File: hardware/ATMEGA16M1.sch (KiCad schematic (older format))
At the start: 44 parts, among them IC1 ATMEGA16M1-A, IC2 MCP2551-I/SN, J1 PWR, J2 USB, J3 RELAY, J4 RELAY, J5 RELAY, J6 GPIO, J7 AMP/D2A, J8 ADC, J9 CAN, SW1 SW_PUSH, U1 NCP1117ST50T3G, U2 FT232RL, U3 RELAY_VO14642AT, U4 RELAY_VO14642AT, U5 RELAY_VO14642AT, X1 16MHz

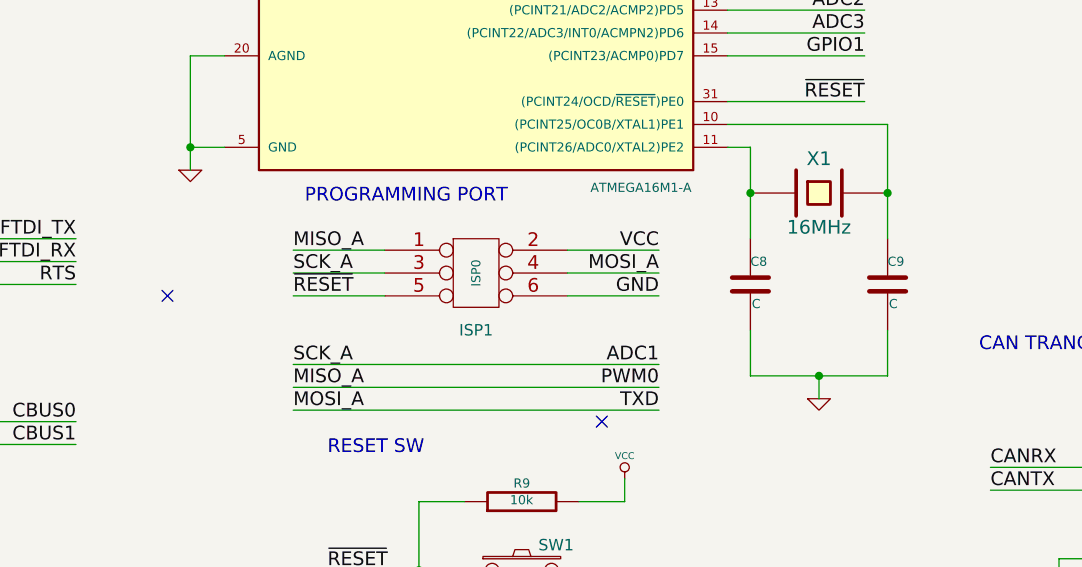
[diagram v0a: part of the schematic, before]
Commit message: PCB revisions: schematic update, cvpcb, pcb component grouping
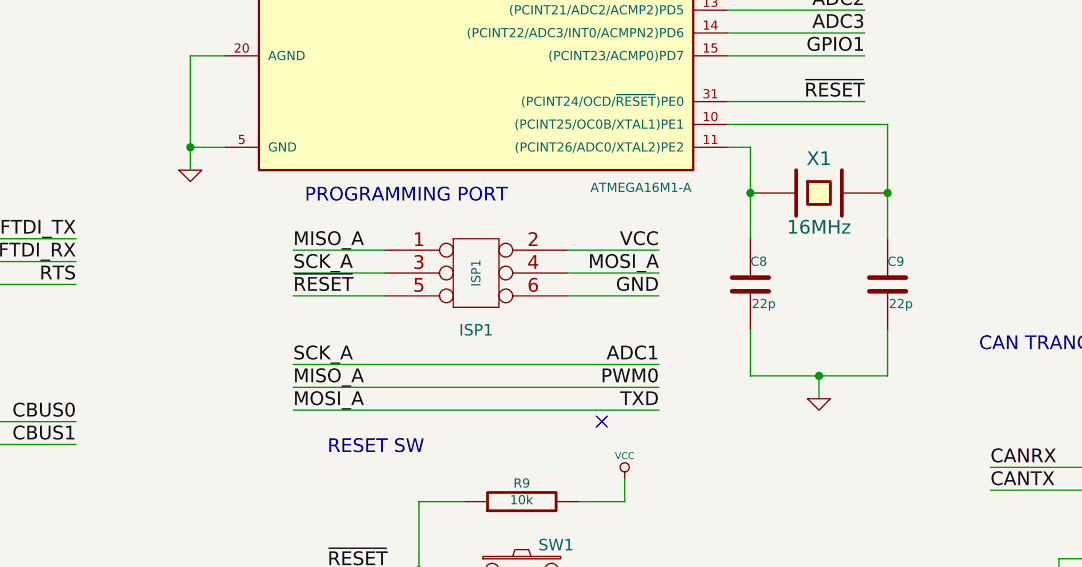
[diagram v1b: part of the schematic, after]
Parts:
- C8, C9: value C -> 22p
- ISP1: value ISP0 -> ISP1
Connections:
- no-connect marks 18 -> 17
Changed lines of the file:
@@
 Sheet 1 1
 Title "LFEF CAN Communication Board"
-Date "10 mar 2015"
+Date "23 mar 2015"
 Rev "0"
 Comp "Lafayette College"
@@
 P 6350 4700
 F 0 "C8" H 6350 4800 40  0000 L CNN
-F 1 "C" H 6356 4615 40  0000 L CNN
+F 1 "22p" H 6356 4615 40  0000 L CNN
 F 2 "~" H 6388 4550 30  0000 C CNN
 F 3 "~" H 6350 4700 60  0000 C CNN
@@
 P 6950 4700
 F 0 "C9" H 6950 4800 40  0000 L CNN
-F 1 "C" H 6956 4615 40  0000 L CNN
+F 1 "22p" H 6956 4615 40  0000 L CNN
 F 2 "~" H 6988 4550 30  0000 C CNN
 F 3 "~" H 6950 4700 60  0000 C CNN
@@
 P 5150 4700
 F 0 "ISP1" H 5150 4500 50  0000 C CNN
-F 1 "ISP0" V 5150 4750 40  0000 C CNN
+F 1 "ISP1" V 5150 4750 40  0000 C CNN
 F 2 "~" H 5150 4700 60  0000 C CNN
 F 3 "~" H 5150 4700 60  0000 C CNN
@@
 I/O HEADERS
 NoConn ~ 9650 4000
-NoConn ~ 3800 4750
 NoConn ~ 5700 5300
 $Comp

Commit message: PCB rough initial layout
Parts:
- added R11, R12, R13: 220, ~, symbol R
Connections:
- net GND: now also J7.8
- net SSR0: now also R11.1; no longer U3.1 (A)
- net SSR1: now also R12.1; no longer U4.1 (A)
- net SSR2: now also R13.1; no longer U5.1 (A)
- new net: R11.2, U3.1 (A)
- new net: R12.2, U4.1 (A)
- new net: R13.2, U5.1 (A)
- no-connect marks 17 -> 16
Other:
- moved on the sheet: U3, U4, U5

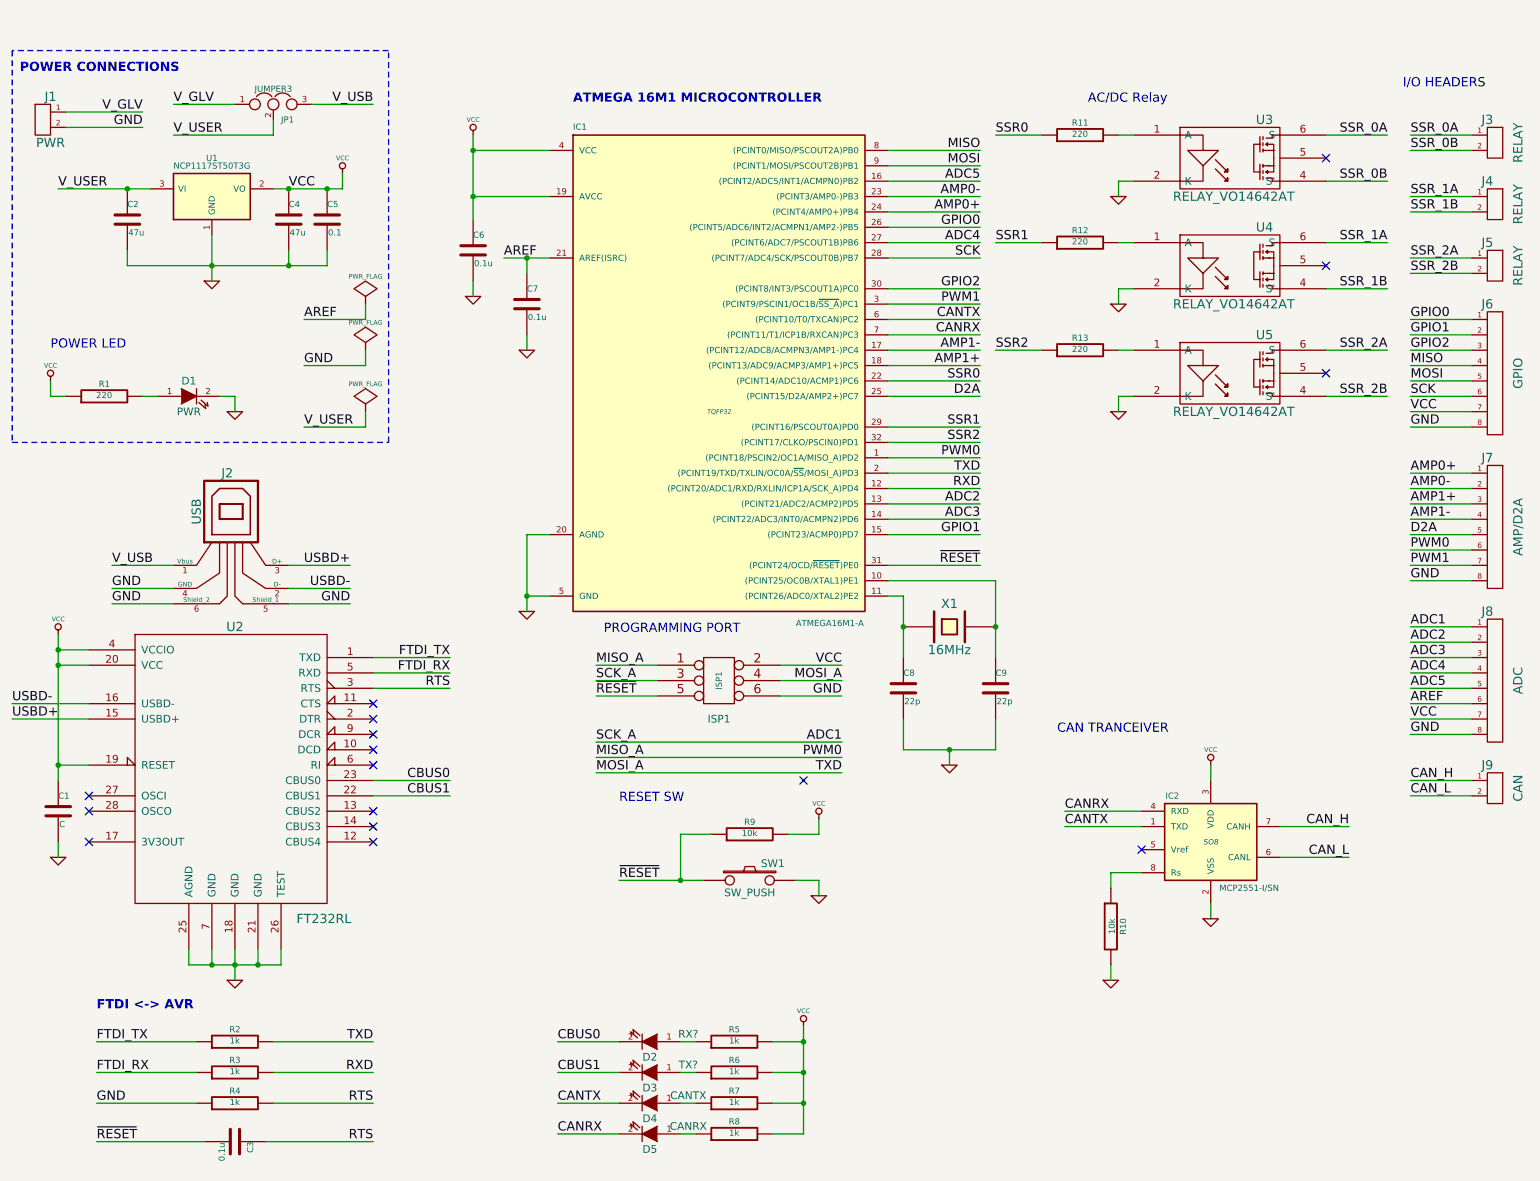
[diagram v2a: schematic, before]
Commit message: PCB physical layout (mostly) complete
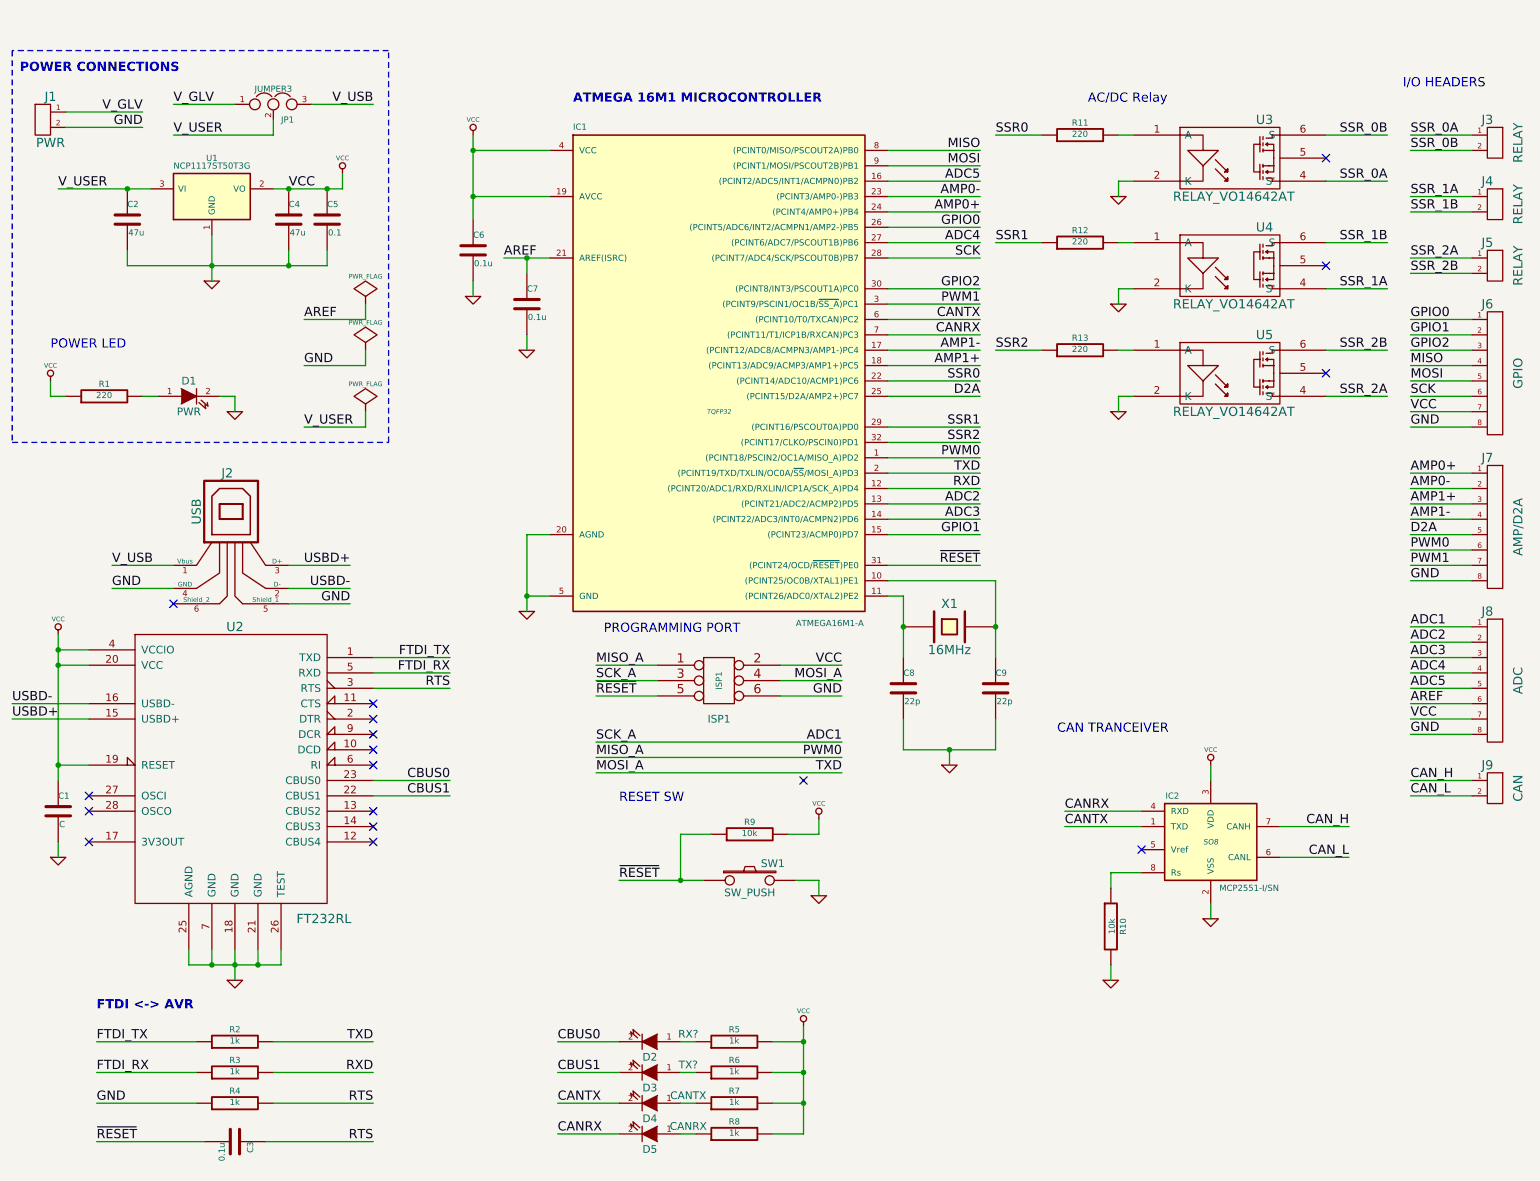
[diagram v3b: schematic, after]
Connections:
- net GND: no longer J2.6 (Shield_2)
- net SSR_0A: now also U3.4 (S'); no longer U3.6 (S)
- net SSR_0B: now also U3.6 (S); no longer U3.4 (S')
- net SSR_1A: now also U4.4 (S'); no longer U4.6 (S)
- net SSR_1B: now also U4.6 (S); no longer U4.4 (S')
- net SSR_2A: now also U5.4 (S'); no longer U5.6 (S)
- net SSR_2B: now also U5.6 (S); no longer U5.4 (S')
- no-connect marks 16 -> 17
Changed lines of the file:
@@
 $EndComp
 $Comp
-L VCC #PWR8
+L VCC #PWR01
 U 1 1 54DAA07E
 P 3550 1100
-F 0 "#PWR8" H 3550 1200 30  0001 C CNN
+F 0 "#PWR01" H 3550 1200 30  0001 C CNN
 F 1 "VCC" H 3550 1200 30  0000 C CNN
 F 2 "" H 3550 1100 60  0000 C CNN
@@
 $EndComp
 $Comp
-L GND #PWR11
+L GND #PWR02
 U 1 1 54DAA08D
 P 3900 4200
-F 0 "#PWR11" H 3900 4200 30  0001 C CNN
+F 0 "#PWR02" H 3900 4200 30  0001 C CNN
 F 1 "GND" H 3900 4130 30  0001 C CNN
 F 2 "" H 3900 4200 60  0000 C CNN
@@
 $EndComp
 $Comp
-L GND #PWR15
+L GND #PWR03
 U 1 1 54DAA197
 P 6650 5200
-F 0 "#PWR15" H 6650 5200 30  0001 C CNN
+F 0 "#PWR03" H 6650 5200 30  0001 C CNN
 F 1 "GND" H 6650 5130 30  0001 C CNN
 F 2 "" H 6650 5200 60  0000 C CNN
@@
 $EndComp
 $Comp
-L VCC #PWR13
+L VCC #PWR04
 U 1 1 54DAA29E
 P 5800 5550
-F 0 "#PWR13" H 5800 5650 30  0001 C CNN
+F 0 "#PWR04" H 5800 5650 30  0001 C CNN
 F 1 "VCC" H 5800 5650 30  0000 C CNN
 F 2 "" H 5800 5550 60  0000 C CNN
@@
 $EndComp
 $Comp
-L GND #PWR14
+L GND #PWR05
 U 1 1 54DAA320
 P 5800 6050
-F 0 "#PWR14" H 5800 6050 30  0001 C CNN
+F 0 "#PWR05" H 5800 6050 30  0001 C CNN
 F 1 "GND" H 5800 5980 30  0001 C CNN
 F 2 "" H 5800 6050 60  0000 C CNN
@@
 $EndComp
 $Comp
-L GND #PWR4
+L GND #PWR06
 U 1 1 54DAA728
 P 1850 2050
-F 0 "#PWR4" H 1850 2050 30  0001 C CNN
+F 0 "#PWR06" H 1850 2050 30  0001 C CNN
 F 1 "GND" H 1850 1980 30  0001 C CNN
 F 2 "" H 1850 2050 60  0000 C CNN
@@
 $EndComp
 $Comp
-L VCC #PWR7
+L VCC #PWR07
 U 1 1 54DAA778
 P 2700 1350
-F 0 "#PWR7" H 2700 1450 30  0001 C CNN
+F 0 "#PWR07" H 2700 1450 30  0001 C CNN
 F 1 "VCC" H 2700 1450 30  0000 C CNN
 F 2 "" H 2700 1350 60  0000 C CNN
@@
 $EndComp
 $Comp
-L VCC #PWR1
+L VCC #PWR08
 U 1 1 54DAF8E1
 P 800 2700
-F 0 "#PWR1" H 800 2800 30  0001 C CNN
+F 0 "#PWR08" H 800 2800 30  0001 C CNN
 F 1 "VCC" H 800 2800 30  0000 C CNN
 F 2 "" H 800 2700 60  0000 C CNN
@@
 $EndComp
 $Comp
-L GND #PWR5
+L GND #PWR09
 U 1 1 54DAF9E0
 P 2000 2900
-F 0 "#PWR5" H 2000 2900 30  0001 C CNN
+F 0 "#PWR09" H 2000 2900 30  0001 C CNN
 F 1 "GND" H 2000 2830 30  0001 C CNN
 F 2 "" H 2000 2900 60  0000 C CNN
@@
 $EndComp
 $Comp
-L GND #PWR9
+L GND #PWR010
 U 1 1 54DBBF13
 P 3550 2150
-F 0 "#PWR9" H 3550 2150 30  0001 C CNN
+F 0 "#PWR010" H 3550 2150 30  0001 C CNN
 F 1 "GND" H 3550 2080 30  0001 C CNN
 F 2 "" H 3550 2150 60  0000 C CNN
@@
 $EndComp
 $Comp
-L GND #PWR16
+L GND #PWR011
 U 1 1 54EEA1CE
 P 7700 6600
-F 0 "#PWR16" H 7700 6600 30  0001 C CNN
+F 0 "#PWR011" H 7700 6600 30  0001 C CNN
 F 1 "GND" H 7700 6530 30  0001 C CNN
 F 2 "" H 7700 6600 60  0000 C CNN
@@
 $EndComp
 $Comp
-L GND #PWR6
+L GND #PWR012
 U 1 1 54EEAF05
 P 2000 6600
-F 0 "#PWR6" H 2000 6600 30  0001 C CNN
+F 0 "#PWR012" H 2000 6600 30  0001 C CNN
 F 1 "GND" H 2000 6530 30  0001 C CNN
 F 2 "" H 2000 6600 60  0000 C CNN
@@
 Text Label 2750 4150 2    60   ~ 0
 GND
-Text Label 1200 4150 0    60   ~ 0
-GND
 Text Label 1200 4050 0    60   ~ 0
 GND
@@
 USBD+
 $Comp
-L VCC #PWR2
+L VCC #PWR013
 U 1 1 54EEB2BF
 P 850 4350
-F 0 "#PWR2" H 850 4450 30  0001 C CNN
+F 0 "#PWR013" H 850 4450 30  0001 C CNN
 F 1 "VCC" H 850 4450 30  0000 C CNN
 F 2 "" H 850 4350 60  0000 C CNN
@@
 CBUS1
 $Comp
-L VCC #PWR12
+L VCC #PWR014
 U 1 1 54EEB52B
 P 5700 6900
-F 0 "#PWR12" H 5700 7000 30  0001 C CNN
+F 0 "#PWR014" H 5700 7000 30  0001 C CNN
 F 1 "VCC" H 5700 7000 30  0000 C CNN
 F 2 "" H 5700 6900 60  0000 C CNN
@@
 $EndComp
 $Comp
-L GND #PWR3
+L GND #PWR015
 U 1 1 54EEB94D
 P 850 5800
-F 0 "#PWR3" H 850 5800 30  0001 C CNN
+F 0 "#PWR015" H 850 5800 30  0001 C CNN
 F 1 "GND" H 850 5730 30  0001 C CNN
 F 2 "" H 850 5800 60  0000 C CNN
@@
 AC/DC Relay
 $Comp
-L GND #PWR17
+L GND #PWR016
 U 1 1 54F3FAF1
 P 7750 1500
-F 0 "#PWR17" H 7750 1500 30  0001 C CNN
+F 0 "#PWR016" H 7750 1500 30  0001 C CNN
 F 1 "GND" H 7750 1430 30  0001 C CNN
 F 2 "" H 7750 1500 60  0000 C CNN
@@
 $EndComp
 $Comp
-L GND #PWR18
+L GND #PWR017
 U 1 1 54F3FBDE
 P 7750 2200
-F 0 "#PWR18" H 7750 2200 30  0001 C CNN
+F 0 "#PWR017" H 7750 2200 30  0001 C CNN
 F 1 "GND" H 7750 2130 30  0001 C CNN
 F 2 "" H 7750 2200 60  0000 C CNN
@@
 Text Label 6950 1100 0    60   ~ 0
 SSR0
+Text Label 9500 1400 2    60   ~ 0
+SSR_0A
 Text Label 9500 1100 2    60   ~ 0
-SSR_0A
-Text Label 9500 1400 2    60   ~ 0
 SSR_0B
 NoConn ~ 9100 1250
+Text Label 9500 2100 2    60   ~ 0
+SSR_1A
 Text Label 9500 1800 2    60   ~ 0
-SSR_1A
-Text Label 9500 2100 2    60   ~ 0
 SSR_1B
 NoConn ~ 9100 1950
-$Comp
-L RELAY_VO14642AT U5
-U 1 1 54F5ECF4
-P 8500 2650
-F 0 "U5" H 8700 2900 60  0000 C CNN
-F 1 "RELAY_VO14642AT" H 8500 2400 60  0000 C CNN
-F 2 "~" H 8500 2650 60  0000 C CNN
-F 3 "~" H 8500 2650 60  0000 C CNN
-	1    8500 2650
-	1    0    0    -1
-$EndComp
-$Comp
-L GND #PWR19
-U 1 1 54F5ECFA
-P 7750 2900
-F 0 "#PWR19" H 7750 2900 30  0001 C CNN
-F 1 "GND" H 7750 2830 30  0001 C CNN
-F 2 "" H 7750 2900 60  0000 C CNN
-F 3 "" H 7750 2900 60  0000 C CNN
-	1    7750 2900
-	1    0    0    -1
-$EndComp
-Text Label 6950 2500 0    60   ~ 0
-SSR2
-Text Label 9500 2500 2    60   ~ 0
-SSR_2A
-Text Label 9500 2800 2    60   ~ 0
-SSR_2B
-NoConn ~ 9100 2650
 $Comp
 L C C7
@@
 $EndComp
 $Comp
-L GND #PWR10
+L GND #PWR018
 U 1 1 54F5EF3F
 P 3900 2500
-F 0 "#PWR10" H 3900 2500 30  0001 C CNN
+F 0 "#PWR018" H 3900 2500 30  0001 C CNN
 F 1 "GND" H 3900 2430 30  0001 C CNN
 F 2 "" H 3900 2500 60  0000 C CNN
@@
 NoConn ~ 5700 5300
 $Comp
-L VCC #PWR20
+L VCC #PWR019
 U 1 1 54FEFECC
 P 8350 5200
-F 0 "#PWR20" H 8350 5300 30  0001 C CNN
+F 0 "#PWR019" H 8350 5300 30  0001 C CNN
 F 1 "VCC" H 8350 5300 30  0000 C CNN
 F 2 "" H 8350 5200 60  0000 C CNN
@@
 $EndComp
 $Comp
-L GND #PWR21
+L GND #PWR020
 U 1 1 54FEFEDB
 P 8350 6200
-F 0 "#PWR21" H 8350 6200 30  0001 C CNN
+F 0 "#PWR020" H 8350 6200 30  0001 C CNN
 F 1 "GND" H 8350 6130 30  0001 C CNN
 F 2 "" H 8350 6200 60  0000 C CNN
@@
 V_USER
 $Comp
-L PWR_FLAG #FLG1
+L PWR_FLAG #FLG021
 U 1 1 54FF0968
 P 2850 2200
-F 0 "#FLG1" H 2850 2295 30  0001 C CNN
+F 0 "#FLG021" H 2850 2295 30  0001 C CNN
 F 1 "PWR_FLAG" H 2850 2380 30  0000 C CNN
 F 2 "" H 2850 2200 60  0000 C CNN
@@
 AREF
 $Comp
-L PWR_FLAG #FLG3
+L PWR_FLAG #FLG022
 U 1 1 54FF0976
 P 2850 2900
-F 0 "#FLG3" H 2850 2995 30  0001 C CNN
+F 0 "#FLG022" H 2850 2995 30  0001 C CNN
 F 1 "PWR_FLAG" H 2850 3080 30  0000 C CNN
 F 2 "" H 2850 2900 60  0000 C CNN
@@
 GPIO1
 $Comp
-L PWR_FLAG #FLG2
+L PWR_FLAG #FLG023
 U 1 1 54FF16FA
 P 2850 2500
-F 0 "#FLG2" H 2850 2595 30  0001 C CNN
+F 0 "#FLG023" H 2850 2595 30  0001 C CNN
 F 1 "PWR_FLAG" H 2850 2680 30  0000 C CNN
 F 2 "" H 2850 2500 60  0000 C CNN
@@
 	2350 4150 2750 4150
 Wire Wire Line
-	1200 4150 1600 4150
-Wire Wire Line
 	1200 4050 1600 4050
 Wire Wire Line
@@
 	7250 1100 6950 1100
 Wire Wire Line
+	9100 1400 9500 1400
+Wire Wire Line
 	9100 1100 9500 1100
 Wire Wire Line
-	9100 1400 9500 1400
+	9100 2100 9500 2100
 Wire Wire Line
 	9100 1800 9500 1800
-Wire Wire Line
-	9100 2100 9500 2100
-Wire Wire Line
-	7850 2800 7750 2800
-Wire Wire Line
-	7750 2800 7750 2900
-Wire Wire Line
-	7250 2500 6950 2500
-Wire Wire Line
-	9100 2500 9500 2500
-Wire Wire Line
-	9100 2800 9500 2800
 Wire Wire Line
 	3900 2000 3900 1900
@@
 	7750 1100 7850 1100
 $Comp
+L R R12
+U 1 1 55161DD0
+P 7500 1800
+F 0 "R12" V 7580 1800 40  0000 C CNN
+F 1 "220" V 7507 1801 40  0000 C CNN
+F 2 "~" V 7430 1800 30  0000 C CNN
+F 3 "~" H 7500 1800 30  0000 C CNN
+	1    7500 1800
+	0    -1   -1   0
+$EndComp
+Wire Wire Line
+	7750 1800 7850 1800
+Text Label 9650 4000 0    60   ~ 0
+GND
+Wire Wire Line
+	7750 2500 7850 2500
+$Comp
 L R R13
 U 1 1 55161DCA
@@
 	0    -1   -1   0
 $EndComp
-$Comp
-L R R12
-U 1 1 55161DD0
-P 7500 1800
-F 0 "R12" V 7580 1800 40  0000 C CNN
-F 1 "220" V 7507 1801 40  0000 C CNN
-F 2 "~" V 7430 1800 30  0000 C CNN
-F 3 "~" H 7500 1800 30  0000 C CNN
-	1    7500 1800
-	0    -1   -1   0
-$EndComp
-Wire Wire Line
-	7750 1800 7850 1800
-Wire Wire Line
-	7750 2500 7850 2500
-Text Label 9650 4000 0    60   ~ 0
-GND
+Wire Wire Line
+	9100 2500 9500 2500
+Wire Wire Line
+	9100 2800 9500 2800
+Wire Wire Line
+	7250 2500 6950 2500
+Wire Wire Line
+	7750 2800 7750 2900
+Wire Wire Line
+	7850 2800 7750 2800
+NoConn ~ 9100 2650
+Text Label 9500 2500 2    60   ~ 0
+SSR_2B
+Text Label 9500 2800 2    60   ~ 0
+SSR_2A
+Text Label 6950 2500 0    60   ~ 0
+SSR2
+$Comp
+L GND #PWR024
+U 1 1 54F5ECFA
+P 7750 2900
+F 0 "#PWR024" H 7750 2900 30  0001 C CNN
+F 1 "GND" H 7750 2830 30  0001 C CNN
+F 2 "" H 7750 2900 60  0000 C CNN
+F 3 "" H 7750 2900 60  0000 C CNN
+	1    7750 2900
+	1    0    0    -1
+$EndComp
+$Comp
+L RELAY_VO14642AT U5
+U 1 1 54F5ECF4
+P 8500 2650
+F 0 "U5" H 8700 2900 60  0000 C CNN
+F 1 "RELAY_VO14642AT" H 8500 2400 60  0000 C CNN
+F 2 "~" H 8500 2650 60  0000 C CNN
+F 3 "~" H 8500 2650 60  0000 C CNN
+	1    8500 2650
+	1    0    0    -1
+$EndComp
+NoConn ~ 1600 4150
 $EndSCHEMATC

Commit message: PCB Prototype Finalized, GERBERs Created, Sent for Fabrication
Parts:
- added D10, D11, D9: DIODE, ~, symbol DIODE
- added D6: RELAY1, ~, symbol LED
- added D7: RELAY2, ~, symbol LED
- added D8: RELAY3, ~, symbol LED
- added R14, R16, R5: 1k, ~, symbol R
- D2: value RX? -> RX
- D3: value TX? -> TX
- SW1: value SW_PUSH -> RESET
- renumbered R5 to R15
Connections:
- net ADC1: now also IC1.13 ((PCINT21/ADC2/ACMP2)PD5), J8.3; no longer ISP1.3, J8.1
- net ADC2: now also IC1.14 ((PCINT22/ADC3/INT0/ACMPN2)PD6), J8.4; no longer IC1.13 ((PCINT21/ADC2/ACMP2)PD5), J8.2
- net ADC3: now also IC1.26 ((PCINT5/ADC6/INT2/ACMPN1/AMP2-)PB5), J8.5; no longer IC1.14 ((PCINT22/ADC3/INT0/ACMPN2)PD6), J8.3
- net ADC4: now also J8.6; no longer J8.4
- net AMP0+: now also J7.2; no longer J7.1
- net AMP0-: now also J7.1; no longer J7.2
- net AMP1+: now also J7.4; no longer J7.3
- net AMP1-: now also J7.3; no longer J7.4
- net AREF: now also J8.1; no longer J8.6
- net CAN_H: now also J9.2; no longer J9.1
- net CAN_L: now also J9.1; no longer J9.2
- net GND: now also J8.2, D6.2 (K), D7.2 (K), D8.2 (K)
- net GPIO0: now also IC1.16 ((PCINT2/ADC5/INT1/ACMPN0)PB2), J6.6; no longer IC1.26 ((PCINT5/ADC6/INT2/ACMPN1/AMP2-)PB5), J6.1
- net GPIO1: now also J6.5; no longer J6.2
- net GPIO2: now also J6.4; no longer J6.3
- net MISO: now also J6.1; no longer J6.4
- net MISO_A: now also J7.7; no longer J7.6
- net MOSI: now also J6.2; no longer J6.5
- net RXD: now also ISP1.3
- net SCK: now also J6.3; no longer J6.6
- net SSR0: now also R14.2
- net SSR1: now also R15.2
- net SSR2: now also R16.2
- net SSR_0A: now also D9.2 (K)
- net SSR_0B: now also D9.1 (A)
- net SSR_1A: now also D10.2 (K)
- net SSR_1B: now also D10.1 (A)
- net SSR_2A: now also D11.2 (K)
- net SSR_2B: now also D11.1 (A)
- net VCC: now also R5.2; no longer R15.2
- net at R15.1: now also D7.1 (A); no longer D2.1 (A)
- removed net ADC5: IC1.16 ((PCINT2/ADC5/INT1/ACMPN0)PB2), J8.5
- net PWM1 renamed PWM0
- net PWM0: now also J7.6; no longer J7.7
- new net: D6.1 (A), R14.1
- new net: D8.1 (A), R16.1
- new net: D2.1 (A), R5.1
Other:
- moved on the sheet: C6, C7, C8, C9, IC1, IC2, ISP1, R10, R11, R12, R13, R15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
